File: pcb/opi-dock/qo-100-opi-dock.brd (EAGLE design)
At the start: 75 x 60 mm, 138 parts, among them CON1 6P-SH-SIDE, CON10 3P-SH-TOP, CON11 3P-SH-TOP, CON12 3P-SH-TOP, CON13 3P-SH-TOP, CON14 3P-SH-TOP, CON15 3P-SH-SIDE, CON16 3P-SH-SIDE, CON17 3P-SH-SIDE, CON18 3P-SH-SIDE, CON19 2P-PH-TOP, CON2 6P-SH-SIDE, CON20 2EDG-2P-5MM, CON3 3P-SH-SIDE, CON4 4P-SH-SIDE, CON5 4P-SH-SIDE, CON6 4P-SH-SIDE, CON7 4P-SH-SIDE, CON8 4P-SH-SIDE, CON9 3P-SH-TOP, Q1 AO3400, U1 ORANGEPIZERO, U10 CP2108, U11 DS2484, U12 LTC4313-1, U13 MCP1525, U14 MIC23155, U15 LT8640S, U16 MCP3221-A0, U2 MCP1703-500, U3 MCP23008, U4 LTC4313-2, U5 ADUM1250, U6 MCP1703-500, U7 MCP23008, U8 LTC4313-2, U9 ADUM1250

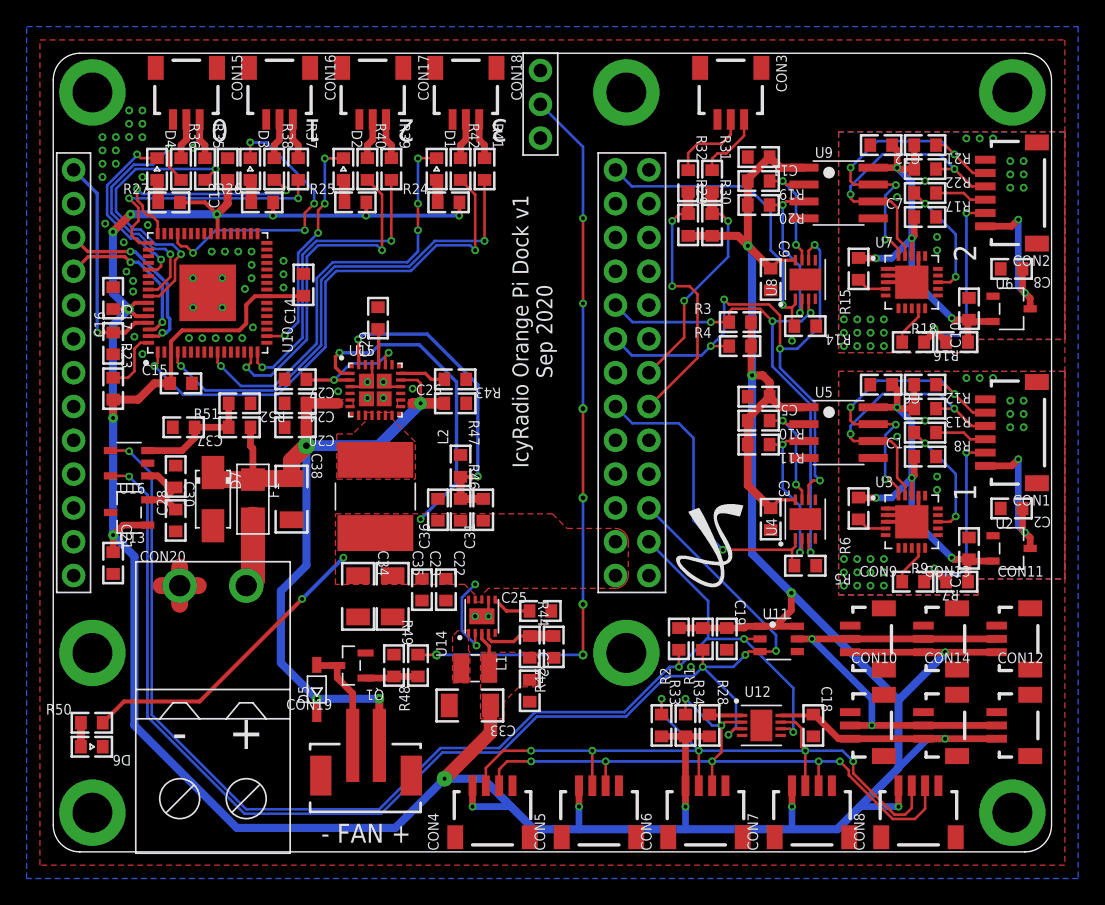
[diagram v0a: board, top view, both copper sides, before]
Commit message: Finish routing OPi dock PCB
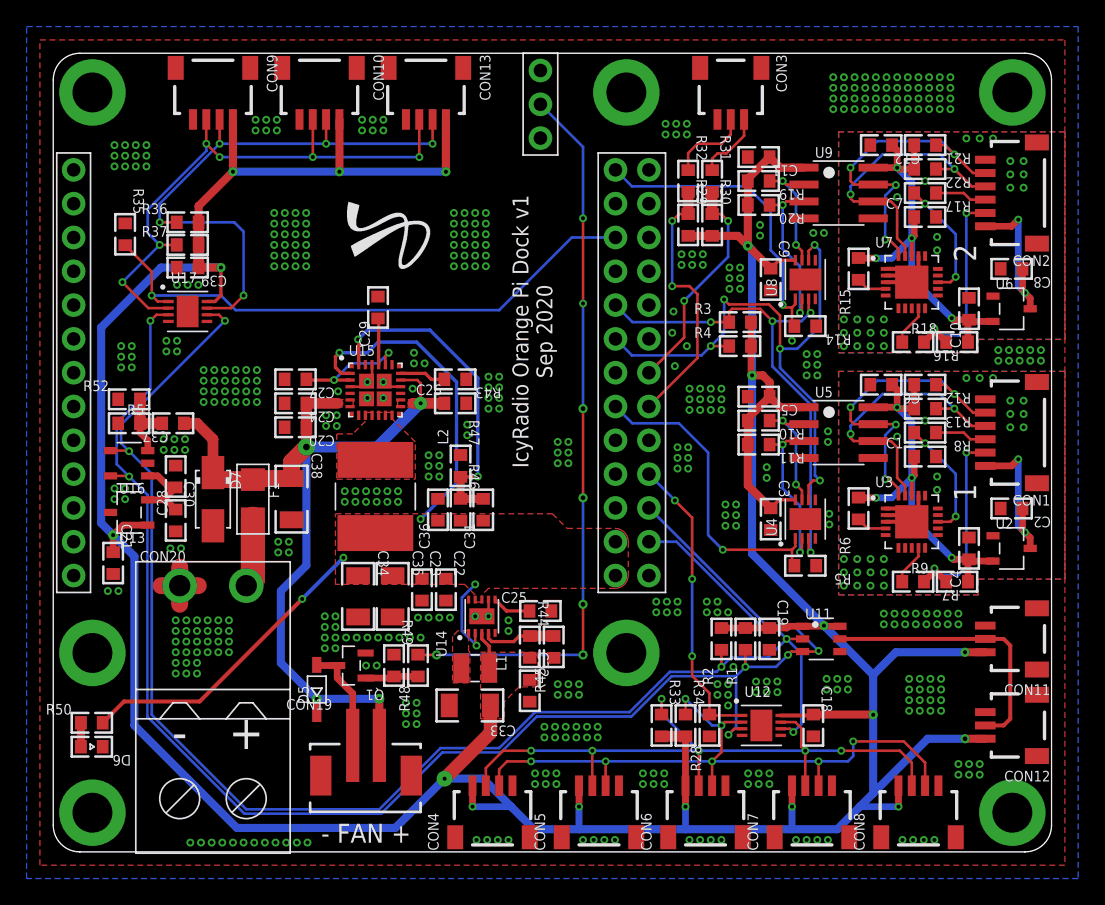
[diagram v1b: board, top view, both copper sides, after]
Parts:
- removed C13, C14, C15, C16, C17: 100nF, Capacitor:CAP0603
- removed CON14: 3P-SH-TOP, JST:SH-03-TOP
- removed CON15, CON16, CON17, CON18: 3P-SH-SIDE, JST:SH-03-SIDE
- removed D1, D2, D3, D4: LED0603, LED:0603
- removed R23: 10K Ohms, Resistor:RES0603
- removed R24, R25, R26, R27: 330 Ohms, Resistor:RES0603
- removed R38, R39, R40, R41, R42: 100 Ohms, Resistor:RES0603
- removed U10: CP2108, Silicon Labs:QFN64
- added C39: 100nF, Capacitor:CAP0603
- added U17: LTC4313-1, Analog Devices:DFN8
- CON10, CON13, CON9: value 3P-SH-TOP -> 4P-SH-SIDE; device JST:SH-03-TOP -> JST:SH-04-SIDE
- CON11, CON12: value 3P-SH-TOP -> 3P-SH-SIDE; device JST:SH-03-TOP -> JST:SH-03-SIDE
- R35: value 100 Ohms -> 10K Ohms
- R36, R37: value 100 Ohms -> 1K Ohms
- moved CON9 64.9 mm to (12.0, 58.0), turned to 180 degrees
- moved CON10 63.8 mm to (20.0, 58.0), turned to 180 degrees
- moved CON13 57.3 mm to (28.0, 58.0), turned to 180 degrees
- moved LOGO1 37.7 mm to (21.9, 49.0), turned to 90 degrees
- moved R37 10.1 mm to (10.1, 45.6), turned to 0 degrees
- moved R52 8.31 mm to (5.70, 34.0), turned to 0 degrees
- moved R35 7.75 mm to (5.40, 46.4)
- moved R51 5.01 mm to (9.00, 32.2)
- moved C37 4.11 mm to (5.70, 32.2)
- moved R36 4.03 mm to (10.1, 47.3), turned to 0 degrees
- moved R1 3.20 mm to (52.0, 16.0)
- moved R2 3.20 mm to (50.2, 16.0)
- moved U11 3.20 mm to (57.7, 16.0)
- moved C19 3.20 mm to (53.8, 16.0)
- moved C29 0.80 mm to (24.4, 40.9)
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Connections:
- net I2C_SCL_EXT renamed I2C_SCL_EXT0
- net I2C_SDA_EXT renamed I2C_SDA_EXT0
- removed net !UART0_ACTIVE: D4.C, U10.53
- removed net !UART1_ACTIVE: D3.C, U10.45
- removed net !UART2_ACTIVE: D2.C, U10.18
- removed net !UART3_ACTIVE: D1.C, U10.10
- removed net N$11: R23.1, U10.64
- removed net N$12: CON15.2, R36.1
- removed net N$13: R28.1, U12.1
- removed net N$14: CON15.1, R35.1
- removed net N$15: D4.A, R27.1
- removed net N$16: CON16.2, R38.1
- removed net N$17: CON16.1, R37.1
- removed net N$18: D3.A, R26.1
- removed net N$20: CON17.2, R40.1
- removed net N$21: CON17.1, R39.1
- removed net N$22: D2.A, R25.1
- removed net N$23: CON18.2, R42.1
- removed net N$24: CON18.1, R41.1
- removed net N$25: D1.A, R24.1
- removed net SBC_USB_DM2: U1.SH$3, U10.63
- removed net SBC_USB_DP2: U1.SH$4, U10.62
- removed net UART0_RX: R36.2, U10.56
- removed net UART0_TX: R35.2, U10.57
- removed net UART1_RX: R38.2, U10.48
- removed net UART1_TX: R37.2, U10.49
- removed net UART2_RX: R40.2, U10.15
- removed net UART2_TX: R39.2, U10.16
- removed net UART3_RX: R42.2, U10.1
- removed net UART3_TX: R41.2, U10.4
- removed net VBUS: C17.1, U1.SH$1, U10.61
- new net EXT_I2C_EN0: R28.2, U1.MH$7, U12.1
- new net EXT_I2C_EN1: R35.2, U1.MH$22, U17.1
- new net I2C_SCL_EXT1: CON10.3, CON13.3, CON9.3, R37.1, U17.2
- new net I2C_SDA_EXT1: CON10.2, CON13.2, CON9.2, R36.1, U17.7
- net 3V3: now also C39.1, R36.2, R37.2, U17.8; no longer C13.1, C14.1, C15.1, C16.1, CON14.1, R23.2, R24.2, R25.2, R26.2, R27.2, R28.2, U10.24, U10.3, U10.39, U10.58, U10.60
- net GND: now also C39.2, CON10.4, CON13.4, CON9.4, R28.1, R35.1, U17.4, U17.9; no longer C13.2, C14.2, C15.2, C16.2, C17.2, CON10.3, CON13.3, CON14.3, CON15.3, CON16.3, CON17.3, CON18.3, CON9.3, U10.2, U10.25, U10.59, U10.65
- net I2C0_SCL: now also U17.3
- net I2C0_SDA: now also U17.6
- net OW_BUS: no longer CON10.2, CON13.2, CON14.2, CON9.2
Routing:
- net I2C_SDA_EXT1: track 0.00 -> 45.1 mm, vias 0 -> 5
- net EXT_I2C_EN1: track 0.00 -> 43.6 mm, vias 0 -> 1
- net I2C_SCL_EXT1: track 0.00 -> 43.2 mm, vias 0 -> 6
- net UART3_RX: track 39.6 -> 0.00 mm, vias 2 -> 0
- net UART3_TX: track 36.8 -> 0.00 mm, vias 2 -> 0
- net 3V3: track 343.2 -> 306.6 mm, vias 20 -> 17
- net !UART3_ACTIVE: track 32.0 -> 0.00 mm, vias 4 -> 0
- net UART2_RX: track 25.3 -> 0.00 mm, vias 2 -> 0
- net UART2_TX: track 23.2 -> 0.00 mm, vias 2 -> 0
- net EXT_I2C_EN0: track 0.00 -> 22.4 mm, vias 0 -> 3
- net !UART1_ACTIVE: track 22.0 -> 0.00 mm, vias 4 -> 0
- net UART0_TX: track 21.9 -> 0.00 mm, vias 2 -> 0
- net I2C0_SDA: track 95.9 -> 117.6 mm, vias 4 -> 5
- net UART0_RX: track 19.8 -> 0.00 mm, vias 2 -> 0
- net UART1_TX: track 18.9 -> 0.00 mm, vias 2 -> 0
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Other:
- board text removed: "0"
- board text removed: "3"
